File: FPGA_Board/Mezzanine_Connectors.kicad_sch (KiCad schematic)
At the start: 1 part

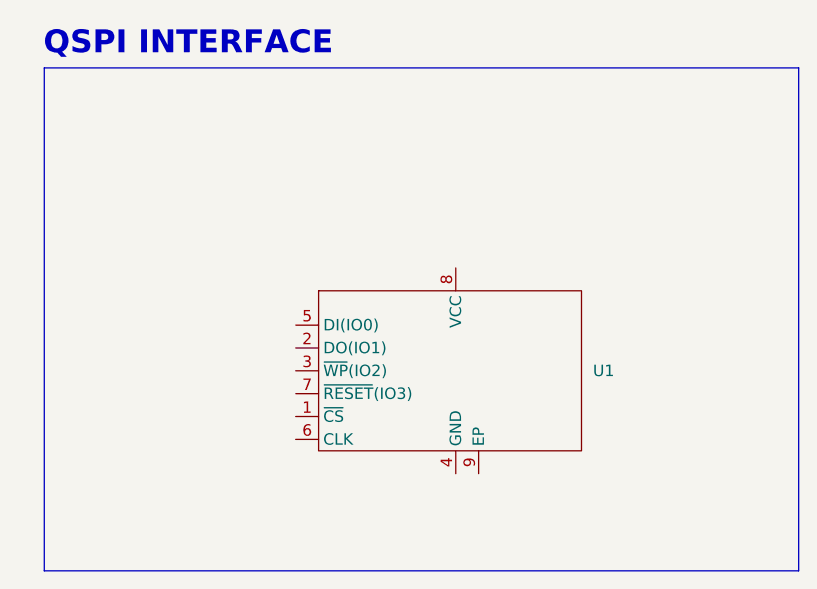
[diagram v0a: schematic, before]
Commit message: Create Block Diagram, create Vivado Project
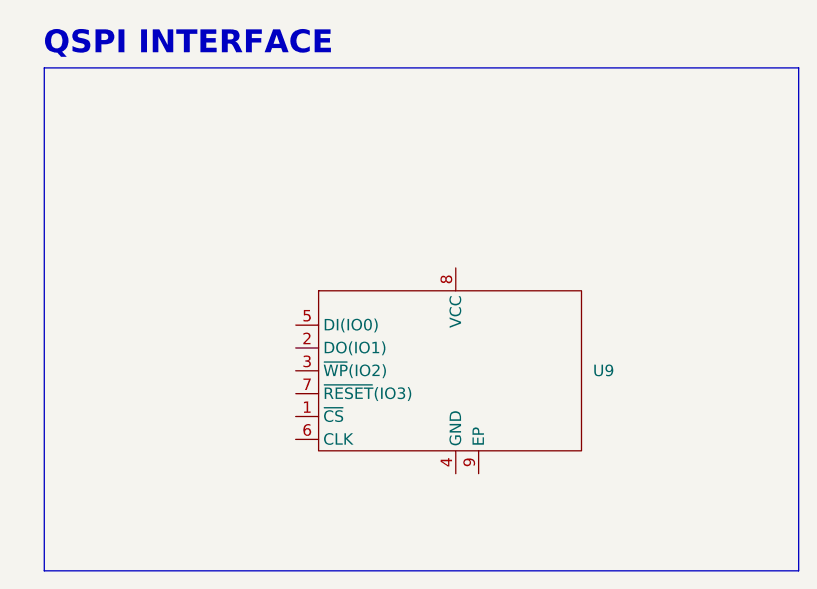
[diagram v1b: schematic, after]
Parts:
- renumbered U1 to U9
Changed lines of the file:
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@@
 		(dnp no)
 		(fields_autoplaced yes)
-		(property "Reference" "U1"
+		(property "Reference" "U9"
 			(at 88.9 161.2899 0)
 			(effects
@@
 		(instances
 			(project "FPGA_Board"
-				(path "/472f09b1-9eb3-4828-aa92-3f9176530a4e/1202234b-3398-4b70-bea7-fa7b5bc7f21a"
-					(reference "U1")
+				(path "/472f09b1-9eb3-4828-aa92-3f9176530a4e/96431787-b88c-488e-8b7c-d91e4e363ff0"
+					(reference "U9")
 					(unit 1)
 				)

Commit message: Create block diagram & QSPI footprint
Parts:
- removed U9: ~, Package_SON:WSON-8-1EP_8x6mm_P1.27mm_EP3.4x4.3mm, symbol FPGA_Parts:W25Q128JVEIQ
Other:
- note removed: "QSPI INTERFACE"
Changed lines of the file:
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@@
 		(company "AUSTIN ADAM")
 	)
-	(rectangle
-		(start 27.94 127.635)
-		(end 111.76 183.515)
-		(stroke
-			(width 0)
-			(type default)
-		)
-		(fill
-			(type none)
-		)
-	)
-	(text "QSPI INTERFACE"
-		(exclude_from_sim no)
-		(at 43.942 124.968 0)
-		(effects
-			(font
-				(size 2.54 2.54)
-				(thickness 0.762)
-				(bold yes)
-			)
-		)
-	)
-	(symbol
-		(lib_id "FPGA_Parts:W25Q128JVEIQ")
-		(at 72.39 161.29 0)
-		(unit 1)
-		(exclude_from_sim no)
-		(in_bom yes)
-		(on_board yes)
-		(dnp no)
-		(fields_autoplaced yes)
-		(property "Reference" "U9"
-			(at 88.9 161.2899 0)
-			(effects
-				(font
-					(size 1.27 1.27)
-				)
-				(justify left)
-			)
-		)
-		(property "Value" "~"
-			(at 72.39 161.29 0)
-			(effects
-				(font
-					(size 1.27 1.27)
-				)
-				(hide yes)
-			)
-		)
-		(property "Footprint" "Package_SON:WSON-8-1EP_8x6mm_P1.27mm_EP3.4x4.3mm"
-			(at 67.056 144.018 0)
-			(effects
-				(font
-					(size 1.27 1.27)
-				)
-				(hide yes)
-			)
-		)
-		(property "Datasheet" "https://www.winbond.com/resource-files/w25q128jv%20revf%2003272018%20plus.pdf"
-			(at 72.39 161.29 0)
-			(effects
-				(font
-					(size 1.27 1.27)
-				)
-				(hide yes)
-			)
-		)
-		(property "Description" "NOR Flash spiFlash, 3V, 128M-bit, 4Kb Uniform Sector"
-			(at 66.04 141.224 0)
-			(effects
-				(font
-					(size 1.27 1.27)
-				)
-				(hide yes)
-			)
-		)
-		(pin "5"
-		)
-		(pin "6"
-		)
-		(pin "4"
-		)
-		(pin "9"
-		)
-		(pin "2"
-		)
-		(pin "3"
-		)
-		(pin "7"
-		)
-		(pin "1"
-		)
-		(pin "8"
-		)
-		(instances
-			(project "FPGA_Board"
-				(path "/472f09b1-9eb3-4828-aa92-3f9176530a4e/96431787-b88c-488e-8b7c-d91e4e363ff0"
-					(reference "U9")
-					(unit 1)
-				)
-			)
-		)
-	)
 )
